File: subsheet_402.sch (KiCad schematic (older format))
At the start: 32 parts, among them J400 DIN-13S — Video Port, Q400 2N3904, Q401 2N3904, Q402 2N3904, Q403 2N3904, U405 74S257_PHY

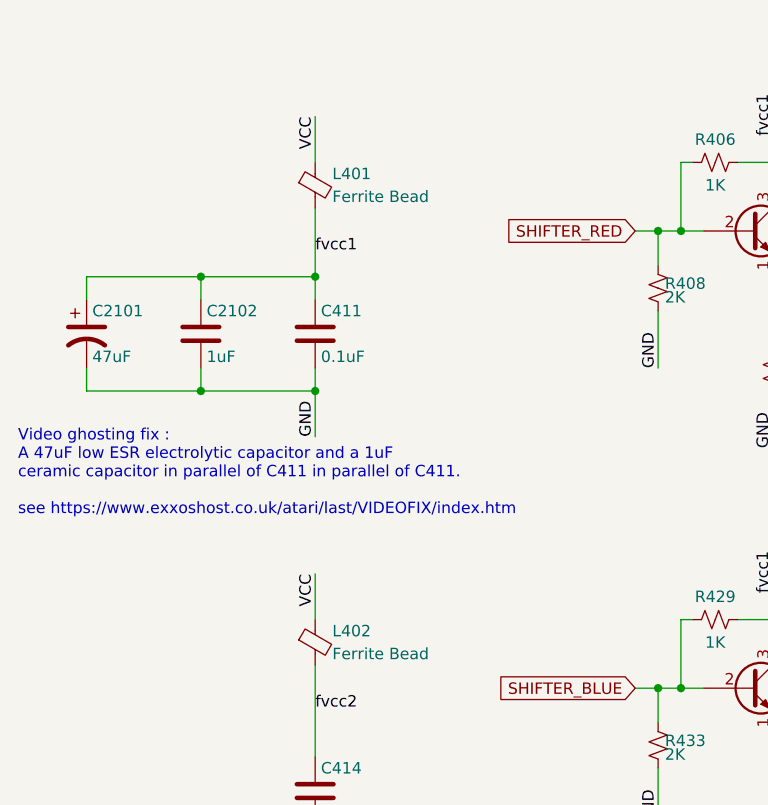
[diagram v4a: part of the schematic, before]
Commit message: Resolves #11 : Use the reference 'FB?' for the ferrite beads
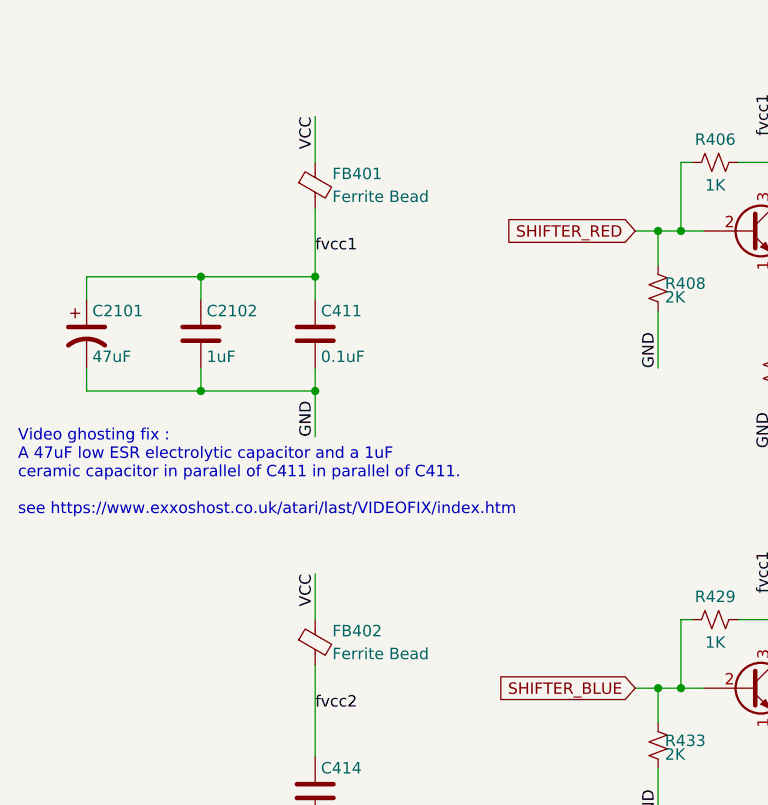
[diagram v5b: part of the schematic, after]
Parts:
- renumbered L401 to FB401, L402 to FB402
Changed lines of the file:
@@
 $EndComp
 $Comp
-L Device:Ferrite_Bead_Small L401
+L Device:Ferrite_Bead_Small FB401
 U 1 1 60B41C5A
 P 2000 3500
-F 0 "L401" H 2075 3550 50  0000 L CNN
+F 0 "FB401" H 2075 3550 50  0000 L CNN
 F 1 "Ferrite Bead" H 2075 3450 50  0000 L CNN
 F 2 "commons_passives_THT:Passive_THT_ferrite_bead_W3.81mm_L15.24mm" V 1930 3500 50  0001 C CNN
@@
 VCC
 $Comp
-L Device:Ferrite_Bead_Small L402
+L Device:Ferrite_Bead_Small FB402
 U 1 1 60B49A84
 P 2000 5500
-F 0 "L402" H 2075 5550 50  0000 L CNN
+F 0 "FB402" H 2075 5550 50  0000 L CNN
 F 1 "Ferrite Bead" H 2075 5450 50  0000 L CNN
 F 2 "commons_passives_THT:Passive_THT_ferrite_bead_W3.81mm_L15.24mm" V 1930 5500 50  0001 C CNN

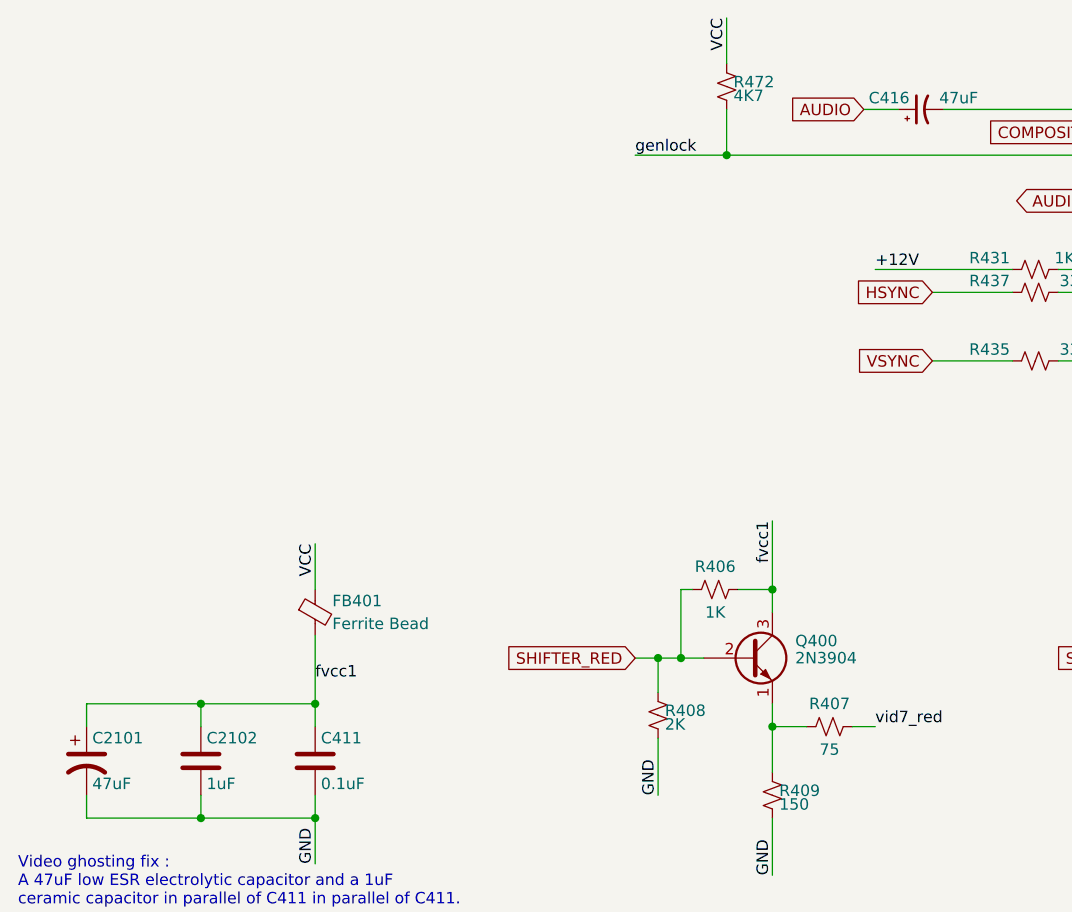
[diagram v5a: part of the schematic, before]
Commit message: Resolves #12 : Use the reference 'CP?' for polarized capacitors
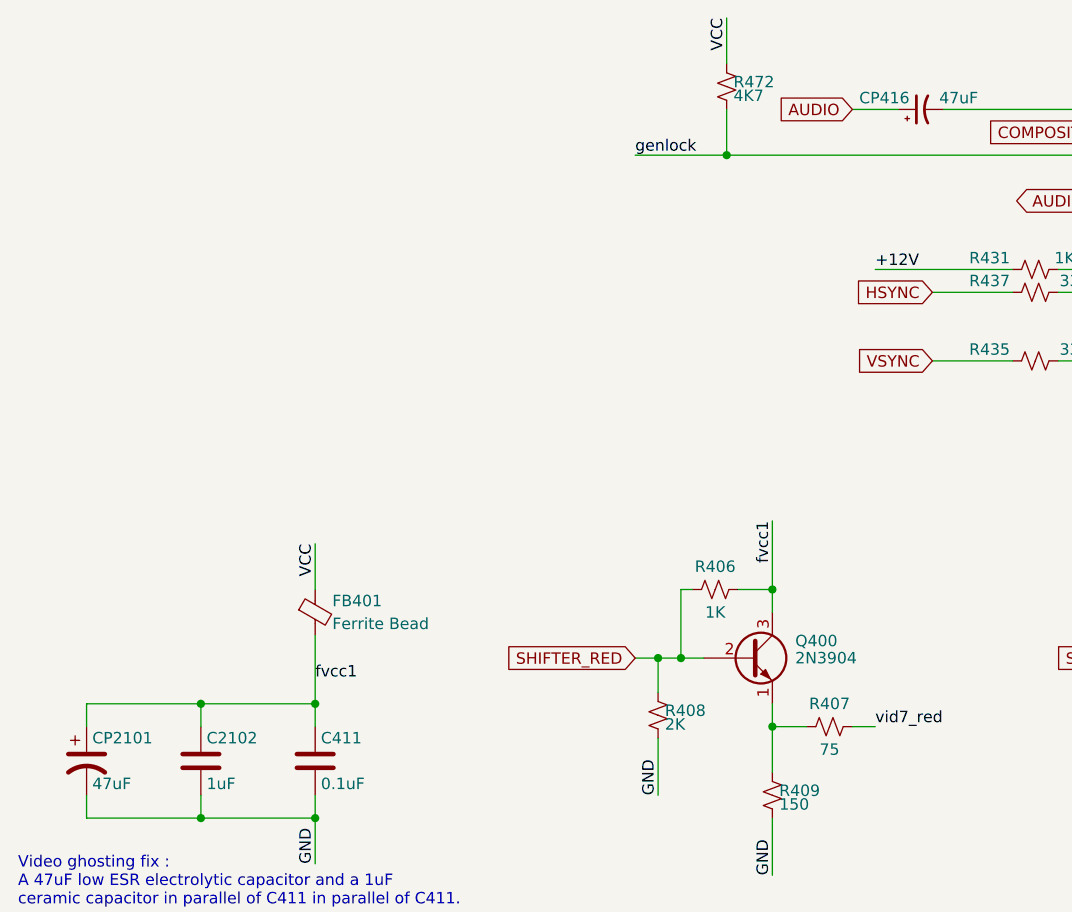
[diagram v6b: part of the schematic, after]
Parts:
- renumbered C2101 to CP2101, C416 to CP416
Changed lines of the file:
@@
 Wire Wire Line
 	5900 2300 6150 2300
-Text GLabel 4400 1300 0    50   Input ~ 0
+Text GLabel 4350 1300 0    50   Input ~ 0
 AUDIO
 $Comp
-L Device:CP1_Small C416
+L Device:CP1_Small CP416
 U 1 1 60BDD743
 P 4650 1300
-F 0 "C416" V 4700 1350 50  0000 L CNN
+F 0 "CP416" V 4700 1350 50  0000 L CNN
 F 1 "47uF" V 4700 1050 50  0000 L CNN
 F 2 "commons_passives_THT:Passive_THT_capacitor_polarized_rad_D5.08mm_P2.54mm_H12.70mm" H 4650 1300 50  0001 C CNN
@@
 	0    -1   -1   0
 $EndComp
-Wire Wire Line
-	4400 1300 4550 1300
 Text GLabel 5850 1400 0    50   Input ~ 0
 COMPOSITE_OR_CSYNC
@@
 P 1000 4150
 AR Path="/6089D0C2/61CEA8C5" Ref="C?"  Part="1"
-AR Path="/60B3D9E3/61CEA8C5" Ref="C2101"  Part="1"
-F 0 "C2101" H 1025 4250 50  0000 L CNN
+AR Path="/60B3D9E3/61CEA8C5" Ref="CP2101"  Part="1"
+F 0 "CP2101" H 1025 4250 50  0000 L CNN
 F 1 "47uF" H 1025 4050 50  0000 L CNN
 F 2 "commons_passives_THT:Passive_THT_capacitor_polarized_W6.35mm_L20.32mm" H 1000 4150 50  0001 C CNN
@@
 	2000 4400 2000 4300
 Connection ~ 2000 4400
+Wire Wire Line
+	4350 1300 4550 1300
 $EndSCHEMATC

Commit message: Resolves #13 : assign 1206 hand-solder footprints to resistors
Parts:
- R406, R407, R408, R409, R413, R420, R423, R425, R429, R431, R432, R433, R434, R435, R437, R438, R440, R441, R472: footprint commons_passives_THT:Passive_THT_resistor_W2.54mm_L12.70mm -> Resistor_SMD:R_1206_3216Metric_Pad1.30x1.75mm_HandSolder
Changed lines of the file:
@@
 F 0 "R406" V 3650 3400 50  0000 C CNN
 F 1 "1K" V 3850 3400 50  0000 C CNN
-F 2 "commons_passives_THT:Passive_THT_resistor_W2.54mm_L12.70mm" H 3750 3400 50  0001 C CNN
+F 2 "Resistor_SMD:R_1206_3216Metric_Pad1.30x1.75mm_HandSolder" H 3750 3400 50  0001 C CNN
 F 3 "~" H 3750 3400 50  0001 C CNN
 	1    3750 3400
@@
 F 0 "R407" V 4150 4000 50  0000 C CNN
 F 1 "75" V 4350 4000 50  0000 C CNN
-F 2 "commons_passives_THT:Passive_THT_resistor_W2.54mm_L12.70mm" H 4250 4000 50  0001 C CNN
+F 2 "Resistor_SMD:R_1206_3216Metric_Pad1.30x1.75mm_HandSolder" H 4250 4000 50  0001 C CNN
 F 3 "~" H 4250 4000 50  0001 C CNN
 	1    4250 4000
@@
 F 0 "R409" H 4030 4320 50  0000 L CNN
 F 1 "150" H 4030 4260 50  0000 L CNN
-F 2 "commons_passives_THT:Passive_THT_resistor_W2.54mm_L12.70mm" H 4000 4300 50  0001 C CNN
+F 2 "Resistor_SMD:R_1206_3216Metric_Pad1.30x1.75mm_HandSolder" H 4000 4300 50  0001 C CNN
 F 3 "~" H 4000 4300 50  0001 C CNN
 	1    4000 4300
@@
 F 0 "R408" H 3530 3970 50  0000 L CNN
 F 1 "2K" H 3530 3910 50  0000 L CNN
-F 2 "commons_passives_THT:Passive_THT_resistor_W2.54mm_L12.70mm" H 3500 3950 50  0001 C CNN
+F 2 "Resistor_SMD:R_1206_3216Metric_Pad1.30x1.75mm_HandSolder" H 3500 3950 50  0001 C CNN
 F 3 "~" H 3500 3950 50  0001 C CNN
 	1    3500 3950
@@
 F 0 "R413" V 6150 3400 50  0000 C CNN
 F 1 "1K" V 6350 3400 50  0000 C CNN
-F 2 "commons_passives_THT:Passive_THT_resistor_W2.54mm_L12.70mm" H 6250 3400 50  0001 C CNN
+F 2 "Resistor_SMD:R_1206_3216Metric_Pad1.30x1.75mm_HandSolder" H 6250 3400 50  0001 C CNN
 F 3 "~" H 6250 3400 50  0001 C CNN
 	1    6250 3400
@@
 F 0 "R423" H 6030 3970 50  0000 L CNN
 F 1 "2K" H 6030 3910 50  0000 L CNN
-F 2 "commons_passives_THT:Passive_THT_resistor_W2.54mm_L12.70mm" H 6000 3950 50  0001 C CNN
+F 2 "Resistor_SMD:R_1206_3216Metric_Pad1.30x1.75mm_HandSolder" H 6000 3950 50  0001 C CNN
 F 3 "~" H 6000 3950 50  0001 C CNN
 	1    6000 3950
@@
 F 0 "R420" V 6650 4000 50  0000 C CNN
 F 1 "75" V 6850 4000 50  0000 C CNN
-F 2 "commons_passives_THT:Passive_THT_resistor_W2.54mm_L12.70mm" H 6750 4000 50  0001 C CNN
+F 2 "Resistor_SMD:R_1206_3216Metric_Pad1.30x1.75mm_HandSolder" H 6750 4000 50  0001 C CNN
 F 3 "~" H 6750 4000 50  0001 C CNN
 	1    6750 4000
@@
 F 0 "R425" H 6530 4320 50  0000 L CNN
 F 1 "150" H 6530 4260 50  0000 L CNN
-F 2 "commons_passives_THT:Passive_THT_resistor_W2.54mm_L12.70mm" H 6500 4300 50  0001 C CNN
+F 2 "Resistor_SMD:R_1206_3216Metric_Pad1.30x1.75mm_HandSolder" H 6500 4300 50  0001 C CNN
 F 3 "~" H 6500 4300 50  0001 C CNN
 	1    6500 4300
@@
 F 0 "R429" V 3650 5400 50  0000 C CNN
 F 1 "1K" V 3850 5400 50  0000 C CNN
-F 2 "commons_passives_THT:Passive_THT_resistor_W2.54mm_L12.70mm" H 3750 5400 50  0001 C CNN
+F 2 "Resistor_SMD:R_1206_3216Metric_Pad1.30x1.75mm_HandSolder" H 3750 5400 50  0001 C CNN
 F 3 "~" H 3750 5400 50  0001 C CNN
 	1    3750 5400
@@
 F 0 "R433" H 3530 5970 50  0000 L CNN
 F 1 "2K" H 3530 5910 50  0000 L CNN
-F 2 "commons_passives_THT:Passive_THT_resistor_W2.54mm_L12.70mm" H 3500 5950 50  0001 C CNN
+F 2 "Resistor_SMD:R_1206_3216Metric_Pad1.30x1.75mm_HandSolder" H 3500 5950 50  0001 C CNN
 F 3 "~" H 3500 5950 50  0001 C CNN
 	1    3500 5950
@@
 F 0 "R432" V 4150 6000 50  0000 C CNN
 F 1 "75" V 4350 6000 50  0000 C CNN
-F 2 "commons_passives_THT:Passive_THT_resistor_W2.54mm_L12.70mm" H 4250 6000 50  0001 C CNN
+F 2 "Resistor_SMD:R_1206_3216Metric_Pad1.30x1.75mm_HandSolder" H 4250 6000 50  0001 C CNN
 F 3 "~" H 4250 6000 50  0001 C CNN
 	1    4250 6000
@@
 F 0 "R434" H 4030 6320 50  0000 L CNN
 F 1 "150" H 4030 6260 50  0000 L CNN
-F 2 "commons_passives_THT:Passive_THT_resistor_W2.54mm_L12.70mm" H 4000 6300 50  0001 C CNN
+F 2 "Resistor_SMD:R_1206_3216Metric_Pad1.30x1.75mm_HandSolder" H 4000 6300 50  0001 C CNN
 F 3 "~" H 4000 6300 50  0001 C CNN
 	1    4000 6300
@@
 F 0 "R440" H 6030 5970 50  0000 L CNN
 F 1 "1K" H 6030 5910 50  0000 L CNN
-F 2 "commons_passives_THT:Passive_THT_resistor_W2.54mm_L12.70mm" H 6000 5950 50  0001 C CNN
+F 2 "Resistor_SMD:R_1206_3216Metric_Pad1.30x1.75mm_HandSolder" H 6000 5950 50  0001 C CNN
 F 3 "~" H 6000 5950 50  0001 C CNN
 	1    6000 5950
@@
 F 0 "R438" V 6650 6000 50  0000 C CNN
 F 1 "27" V 6850 6000 50  0000 C CNN
-F 2 "commons_passives_THT:Passive_THT_resistor_W2.54mm_L12.70mm" H 6750 6000 50  0001 C CNN
+F 2 "Resistor_SMD:R_1206_3216Metric_Pad1.30x1.75mm_HandSolder" H 6750 6000 50  0001 C CNN
 F 3 "~" H 6750 6000 50  0001 C CNN
 	1    6750 6000
@@
 F 0 "R441" H 6530 6320 50  0000 L CNN
 F 1 "100" H 6530 6260 50  0000 L CNN
-F 2 "commons_passives_THT:Passive_THT_resistor_W2.54mm_L12.70mm" H 6500 6300 50  0001 C CNN
+F 2 "Resistor_SMD:R_1206_3216Metric_Pad1.30x1.75mm_HandSolder" H 6500 6300 50  0001 C CNN
 F 3 "~" H 6500 6300 50  0001 C CNN
 	1    6500 6300
@@
 F 0 "R431" V 5100 1800 50  0000 C CNN
 F 1 "1K2" V 5100 2150 50  0000 C CNN
-F 2 "commons_passives_THT:Passive_THT_resistor_W2.54mm_L12.70mm" H 5150 2000 50  0001 C CNN
+F 2 "Resistor_SMD:R_1206_3216Metric_Pad1.30x1.75mm_HandSolder" H 5150 2000 50  0001 C CNN
 F 3 "~" H 5150 2000 50  0001 C CNN
 	1    5150 2000
@@
 F 0 "R437" V 5100 1900 50  0000 C CNN
 F 1 "33" V 5100 2250 50  0000 C CNN
-F 2 "commons_passives_THT:Passive_THT_resistor_W2.54mm_L12.70mm" H 5150 2100 50  0001 C CNN
+F 2 "Resistor_SMD:R_1206_3216Metric_Pad1.30x1.75mm_HandSolder" H 5150 2100 50  0001 C CNN
 F 3 "~" H 5150 2100 50  0001 C CNN
 	1    5150 2100
@@
 F 0 "R435" V 5100 2200 50  0000 C CNN
 F 1 "33" V 5100 2550 50  0000 C CNN
-F 2 "commons_passives_THT:Passive_THT_resistor_W2.54mm_L12.70mm" H 5150 2400 50  0001 C CNN
+F 2 "Resistor_SMD:R_1206_3216Metric_Pad1.30x1.75mm_HandSolder" H 5150 2400 50  0001 C CNN
 F 3 "~" H 5150 2400 50  0001 C CNN
 	1    5150 2400
@@
 F 0 "R472" H 3830 1220 50  0000 L CNN
 F 1 "4K7" H 3830 1160 50  0000 L CNN
-F 2 "commons_passives_THT:Passive_THT_resistor_W2.54mm_L12.70mm" H 3800 1200 50  0001 C CNN
+F 2 "Resistor_SMD:R_1206_3216Metric_Pad1.30x1.75mm_HandSolder" H 3800 1200 50  0001 C CNN
 F 3 "~" H 3800 1200 50  0001 C CNN
 	1    3800 1200
